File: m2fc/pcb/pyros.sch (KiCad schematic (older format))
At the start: 28 parts

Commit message: update more bits on flight computer..
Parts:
- added TP? (x2): TESTPAD, symbol TESTPAD
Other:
- note added: "PYROTECHNIC CHANNELS"
- moved on the sheet: C?, D?, P?, Q?, R?

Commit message: fix all the erc errors
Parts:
- gave numbers to parts that had none: 30
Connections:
- net labels added: +3.3V
- net labels removed: VCC

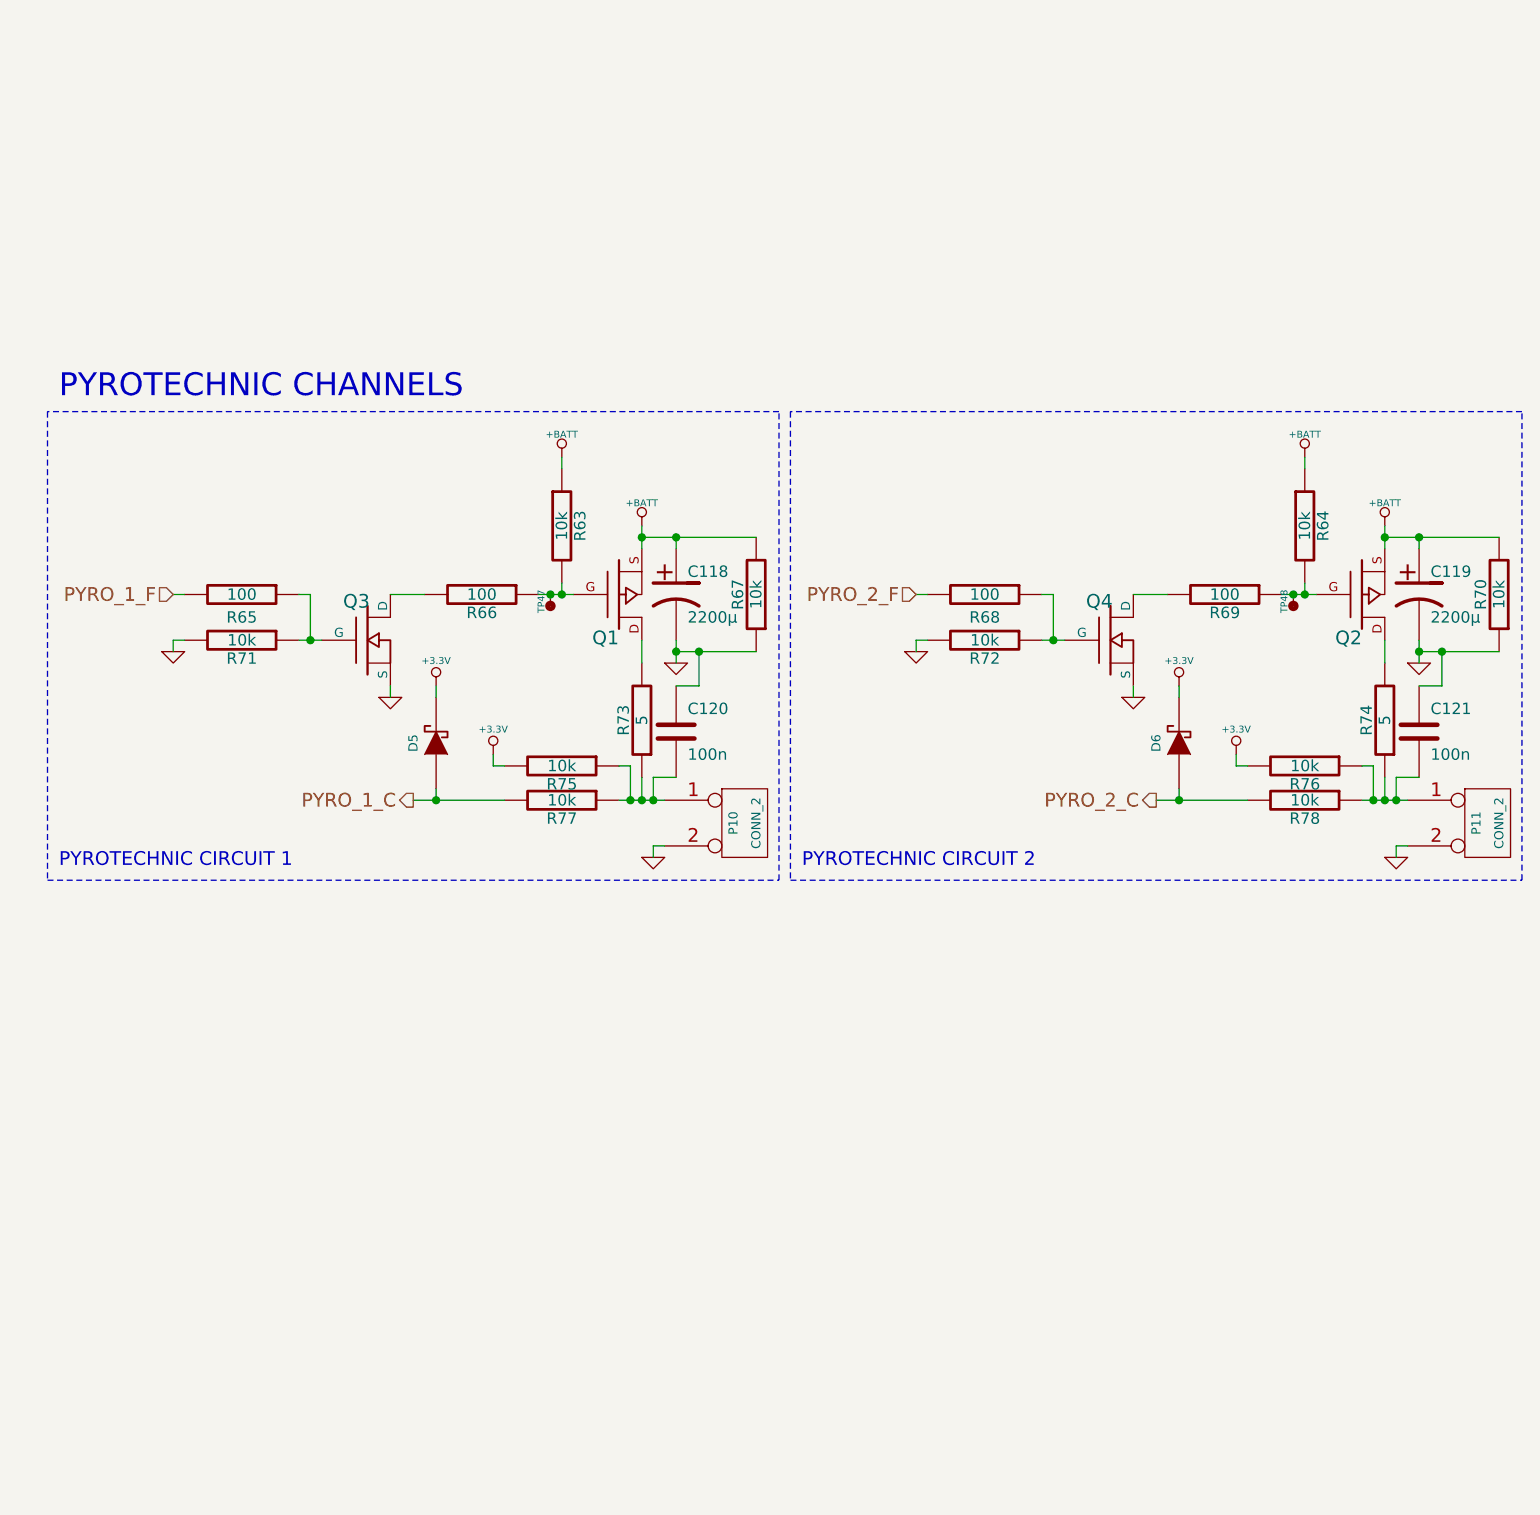
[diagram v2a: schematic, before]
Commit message: update m2fc sch with 3rd pyro and SJs
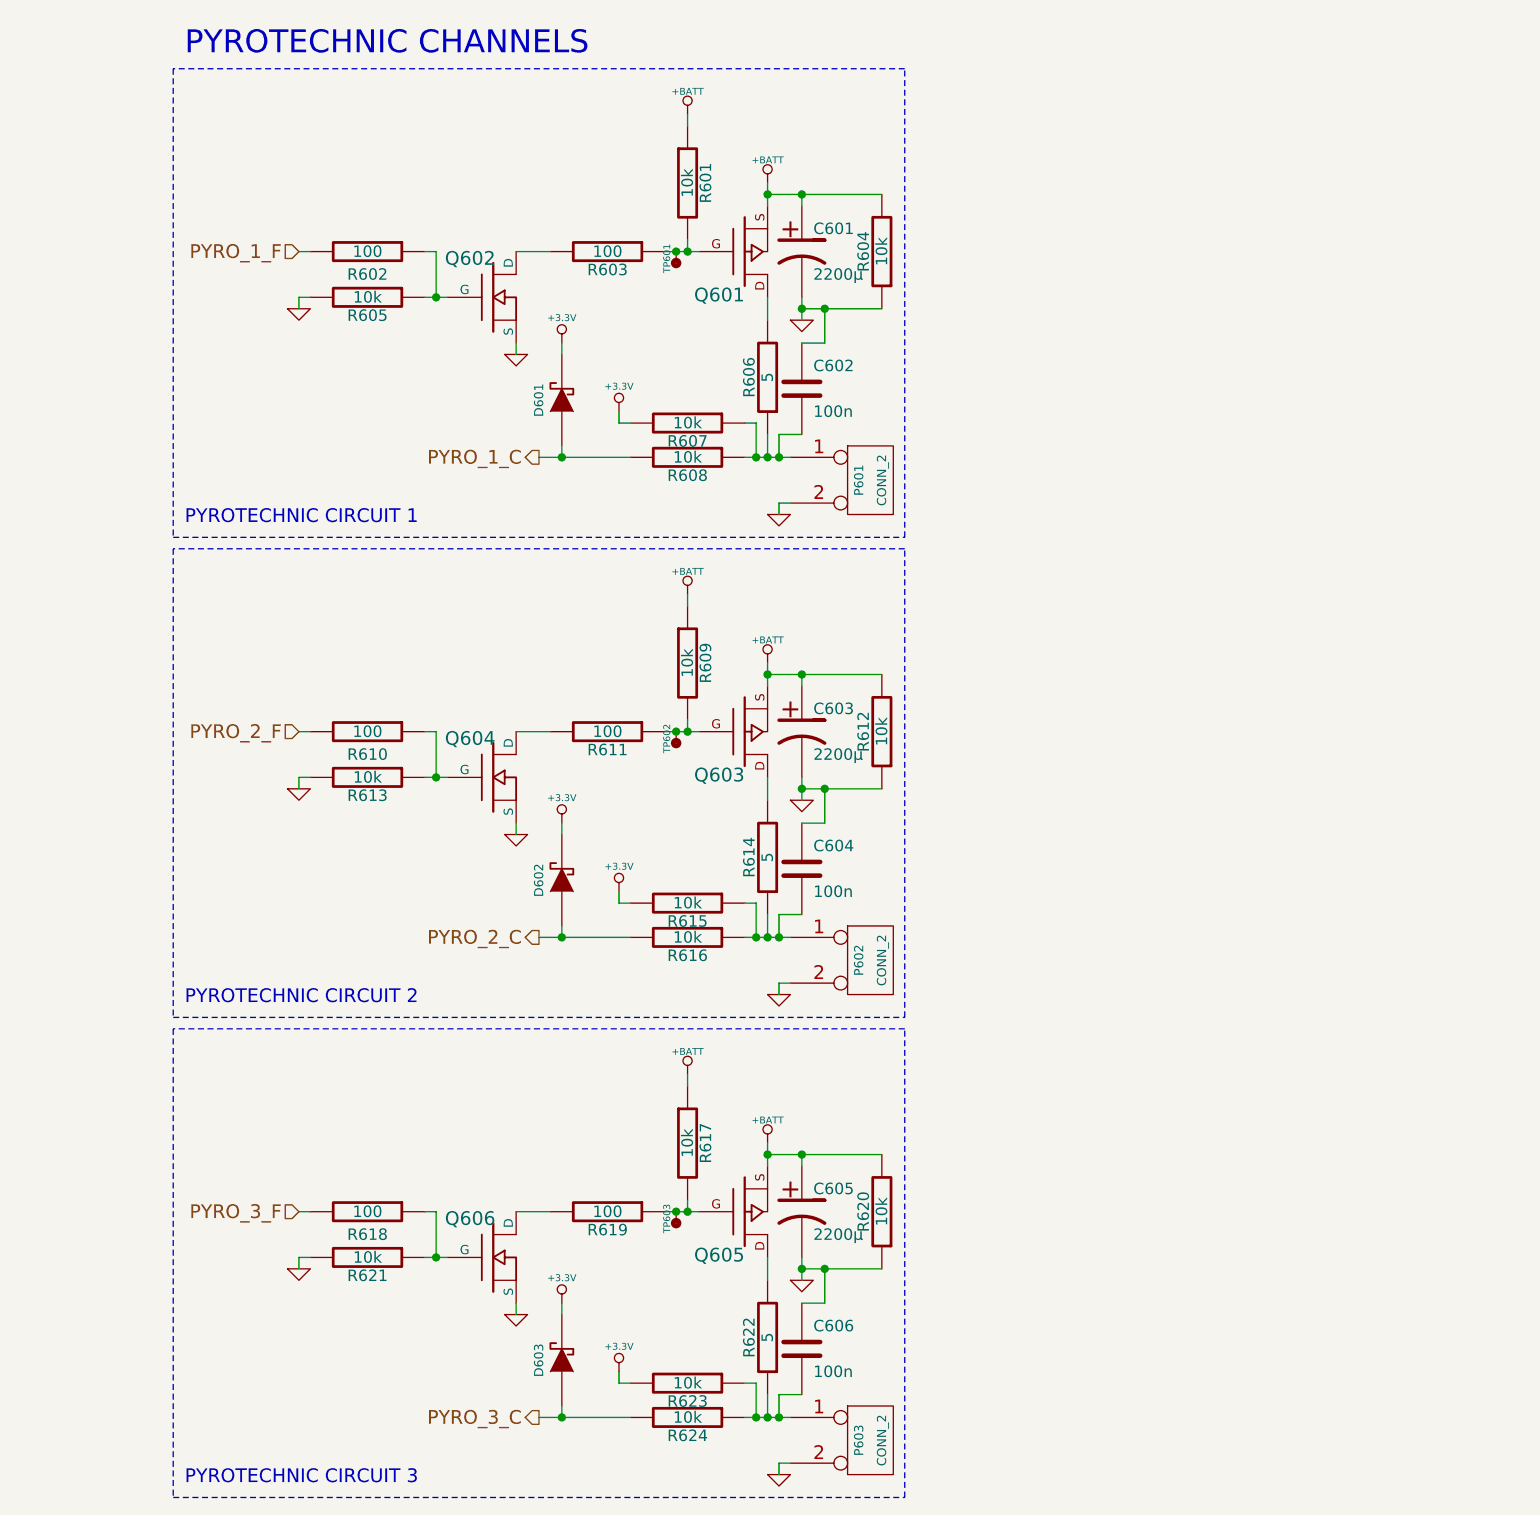
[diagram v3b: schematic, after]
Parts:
- added C605: 2200µ, symbol CP1
- added C606: 100n, 0603, symbol C
- added D603: DIODESCH, SOT-23, symbol DIODESCH
- added P603: CONN_2, symbol CONN_2
- added Q605: MOSFET_P, SOT-23, symbol MOSFET_P
- added Q606: MOSFET_N, SOT-23, symbol MOSFET_N
- added R617, R620, R621, R623, R624: 10k, 0603, symbol R
- added R618, R619: 100, 0603, symbol R
- added R622: 5, symbol R
- added TP603: TESTPAD, symbol TESTPAD
- renumbered C118 to C601, C120 to C602, C119 to C603, C121 to C604, D5 to D601, D6 to D602, P10 to P601, P11 to P602, Q1 to Q601, Q3 to Q602, Q2 to Q603, Q4 to Q604, R63 to R601, R65 to R602, R66 to R603, R67 to R604, R71 to R605, R73 to R606, R75 to R607, R77 to R608, R64 to R609, R68 to R610, R69 to R611, R70 to R612, R72 to R613, R74 to R614, R76 to R615, R78 to R616, TP47 to TP601, TP48 to TP602
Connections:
- net +3.3V: now also D603.2 (K), R623.2
- net +BATT: now also C605.1, Q605.S, R617.1, R620.2
- net GND: now also C605.2, C606.1, P603.2 (PM), Q606.S, R620.1, R621.2
- new net: Q606.G, R618.1, R621.1
- new net: C606.2, P603.1 (P1), R622.1, R623.1, R624.1
- new net: Q605.D, R622.2
- new net: Q605.G, R617.2, R619.1, TP603.1 (TP)
- new net: Q606.D, R619.2
- new net PYRO_3_C: D603.1 (A), R624.2
- new net PYRO_3_F: R618.2
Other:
- note added: "PYROTECHNIC CIRCUIT 3"
- moved on the sheet: C601, C602, C603, C604, D601, D602, P601, P602, Q601, Q602, Q603, Q604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

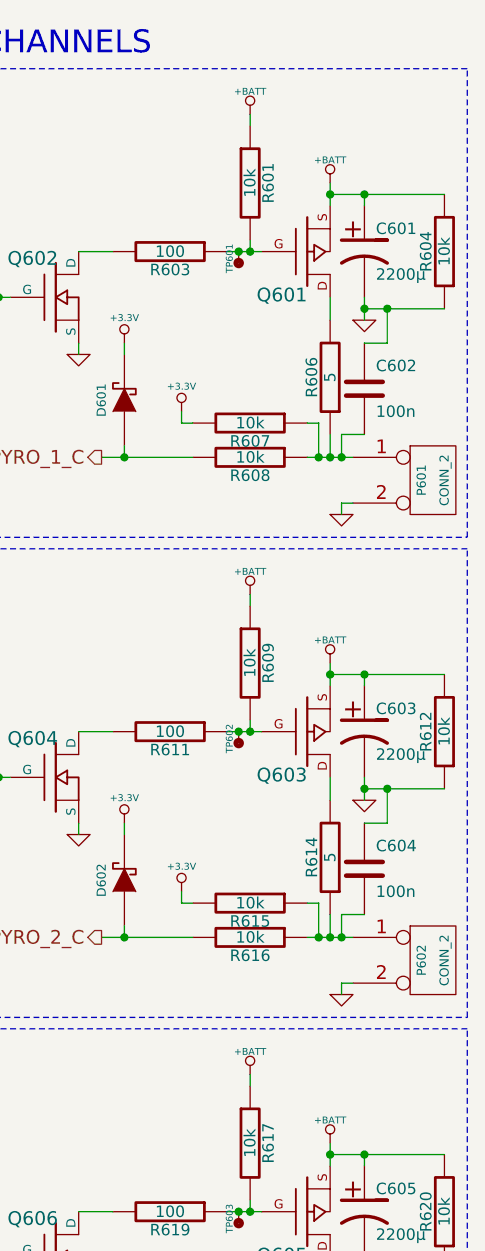
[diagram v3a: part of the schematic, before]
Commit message: swap to JST PA range connectors
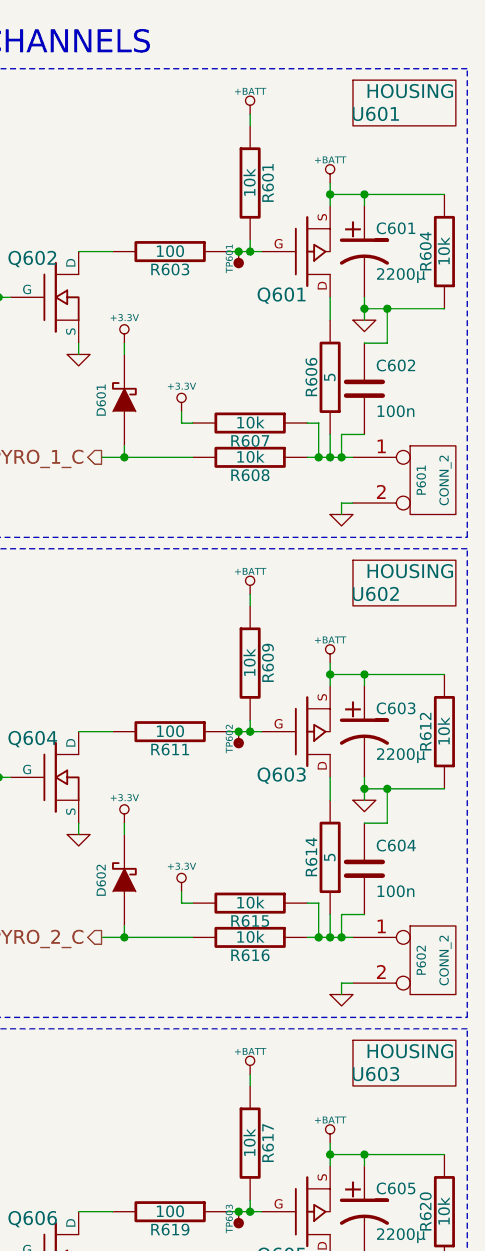
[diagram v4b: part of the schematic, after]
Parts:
- added U601, U602, U603: HOUSING, symbol PART
- P601, P602, P603: Farnell 1462926 -> 1830747
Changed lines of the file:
@@
 F 2 "" H 6150 2850 60  0001 C CNN
 F 3 "" H 6150 2850 60  0001 C CNN
-F 4 "1462926" V 6150 2850 60  0001 C CNN "Farnell"
+F 4 "1830747" V 6150 2850 60  0001 C CNN "Farnell"
 	1    6150 2850
 	1    0    0    -1
@@
 F 2 "" H 6150 4950 60  0001 C CNN
 F 3 "" H 6150 4950 60  0001 C CNN
-F 4 "1462926" V 6150 4950 60  0001 C CNN "Farnell"
+F 4 "1830747" V 6150 4950 60  0001 C CNN "Farnell"
 	1    6150 4950
 	1    0    0    -1
@@
 F 2 "" H 6150 7050 60  0001 C CNN
 F 3 "" H 6150 7050 60  0001 C CNN
-F 4 "1462926" V 6150 7050 60  0001 C CNN "Farnell"
+F 4 "1830747" V 6150 7050 60  0001 C CNN "Farnell"
 	1    6150 7050
 	1    0    0    -1
@@
 	1    0    0    -1
 $EndComp
+$Comp
+L PART U601
+U 1 1 53CE9CFD
+P 5850 1250
+F 0 "U601" H 5900 1250 60  0000 C CNN
+F 1 "HOUSING" H 6050 1350 60  0000 C CNN
+F 2 "" H 5850 1250 60  0000 C CNN
+F 3 "" H 5850 1250 60  0000 C CNN
+F 4 "1830726" H 5850 1250 60  0001 C CNN "Farnell"
+	1    5850 1250
+	1    0    0    -1
+$EndComp
+$Comp
+L PART U602
+U 1 1 53CE9D61
+P 5850 3350
+F 0 "U602" H 5900 3350 60  0000 C CNN
+F 1 "HOUSING" H 6050 3450 60  0000 C CNN
+F 2 "" H 5850 3350 60  0000 C CNN
+F 3 "" H 5850 3350 60  0000 C CNN
+F 4 "1830726" H 5850 3350 60  0001 C CNN "Farnell"
+	1    5850 3350
+	1    0    0    -1
+$EndComp
+$Comp
+L PART U603
+U 1 1 53CEA106
+P 5850 5450
+F 0 "U603" H 5900 5450 60  0000 C CNN
+F 1 "HOUSING" H 6050 5550 60  0000 C CNN
+F 2 "" H 5850 5450 60  0000 C CNN
+F 3 "" H 5850 5450 60  0000 C CNN
+F 4 "1830726" H 5850 5450 60  0001 C CNN "Farnell"
+	1    5850 5450
+	1    0    0    -1
+$EndComp
